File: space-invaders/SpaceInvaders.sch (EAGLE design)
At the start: 26 parts

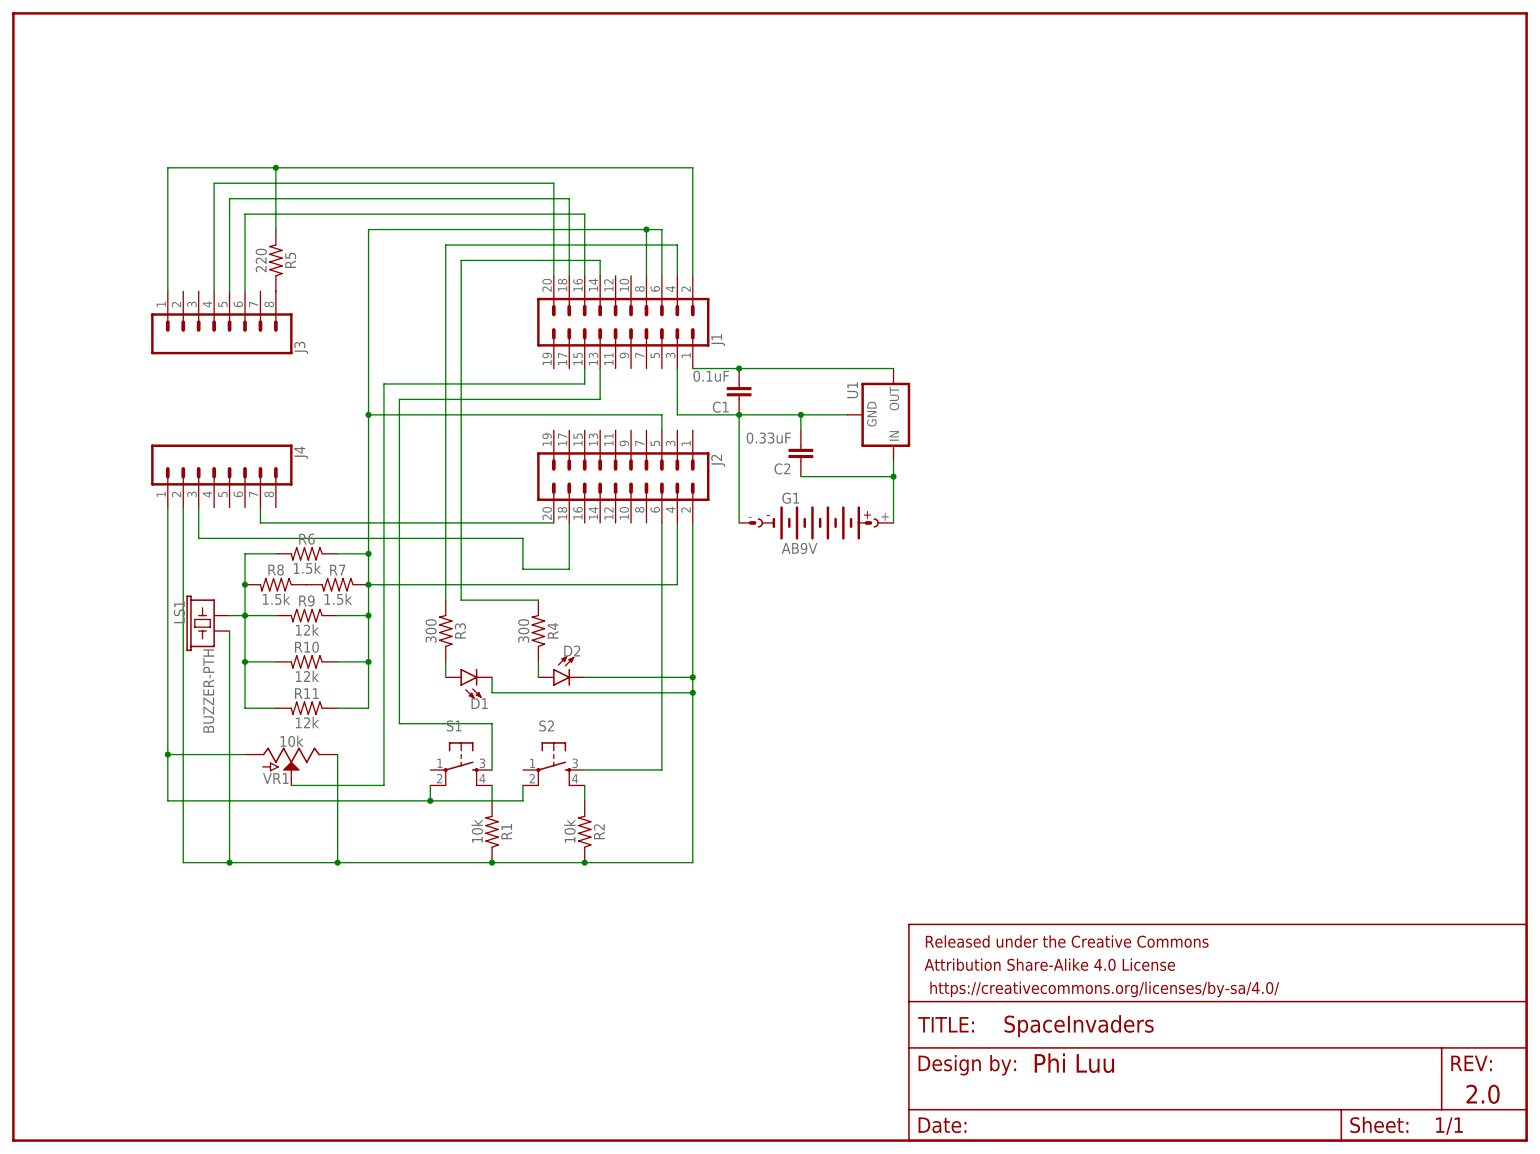
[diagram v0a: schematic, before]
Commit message: Complete board - SpaceInvaders 2.0
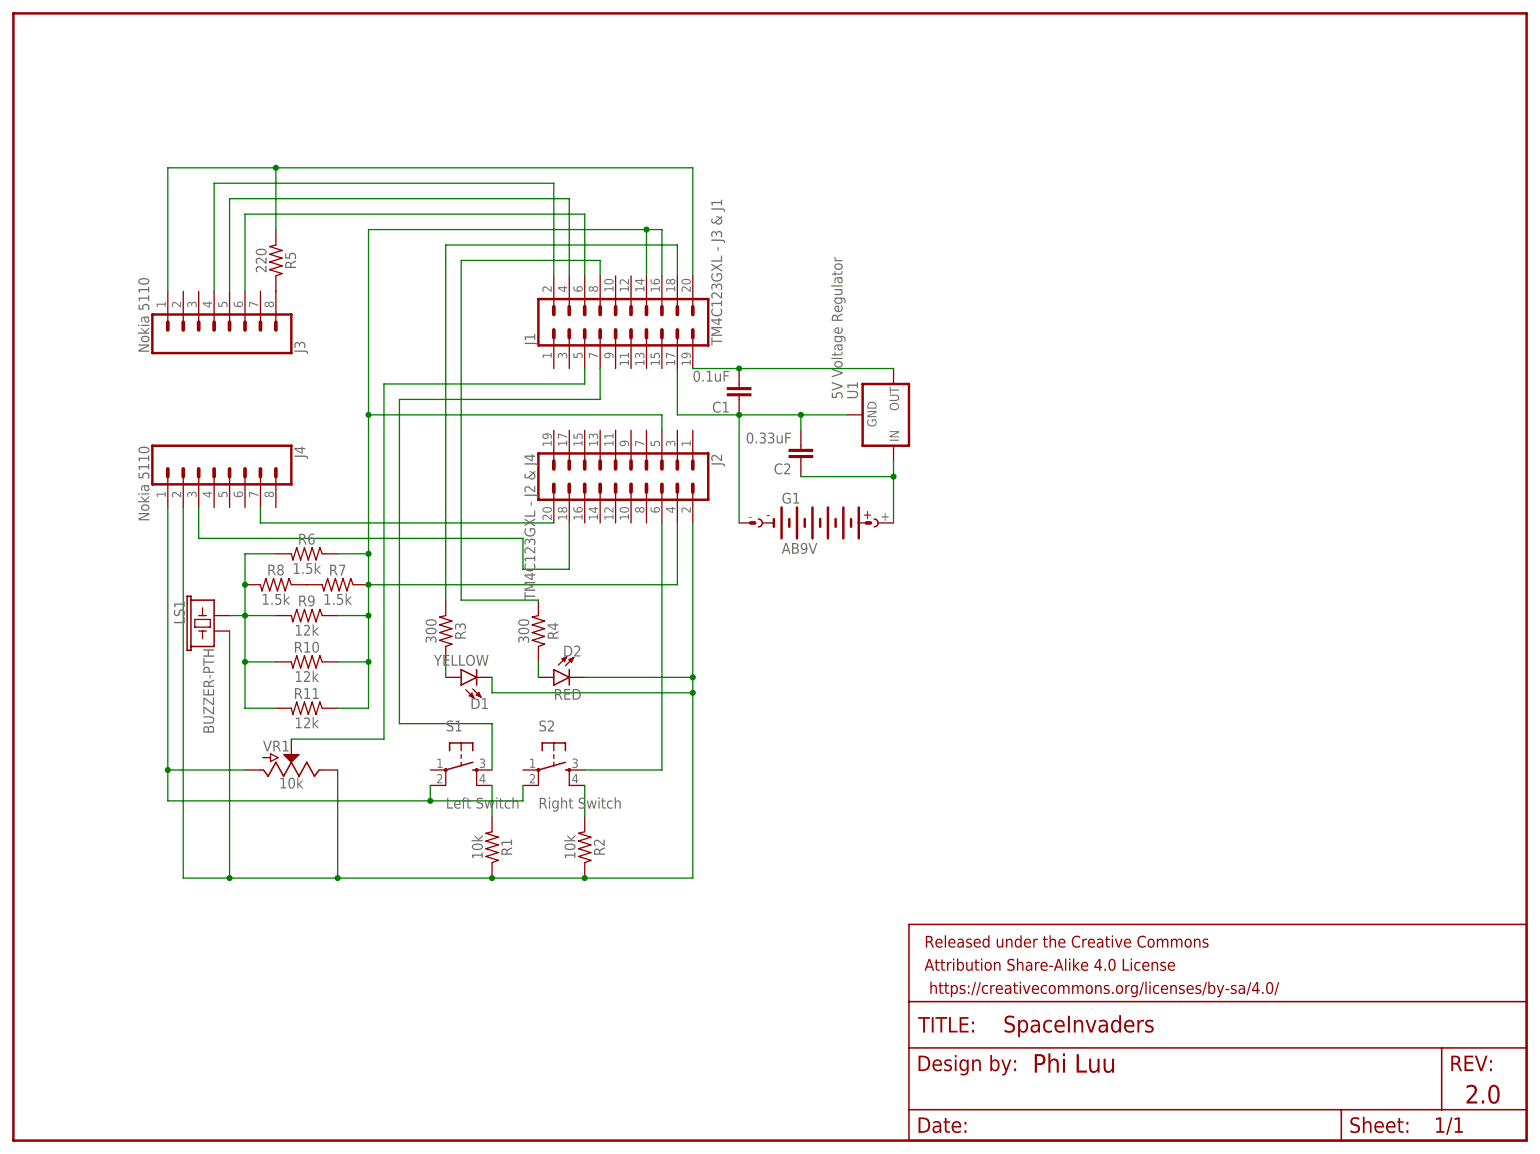
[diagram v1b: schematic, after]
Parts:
- D1: value (none) -> YELLOW; device SparkFun-LED:LED3MM -> SparkFun-LED:LED5MM
- D2: value (none) -> RED; device SparkFun-LED:LED3MM -> SparkFun-LED:LED5MM
- J1: value (none) -> TM4C123GXL - J3 & J1
- J2: value (none) -> TM4C123GXL - J2 & J4
- J3, J4: value (none) -> Nokia 5110
- S1: value (none) -> Left Switch
- S2: value (none) -> Right Switch
- U1: value (none) -> 5V Voltage Regulator
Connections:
- net N$12: now also J1.2; no longer J1.20
- net N$13: now also J1.4; no longer J1.18
- net N$15: now also J1.6; no longer J1.16
- net N$17: now also J1.5; no longer J1.15
- net N$19: now also J1.7; no longer J1.13
- net N$21: now also J1.18; no longer J1.4
- net N$22: now also J1.8; no longer J1.14
- net N$24: now also J1.19; no longer J1.1
- net N$25: now also J1.17; no longer J1.3
- net N$5: now also J1.14, J1.16; no longer J1.6, J1.8
- net N$9: now also J1.20; no longer J1.2
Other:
- moved on the sheet: R1, R2, VR1

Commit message: Add silkscreen & Finish SpaceInvaders
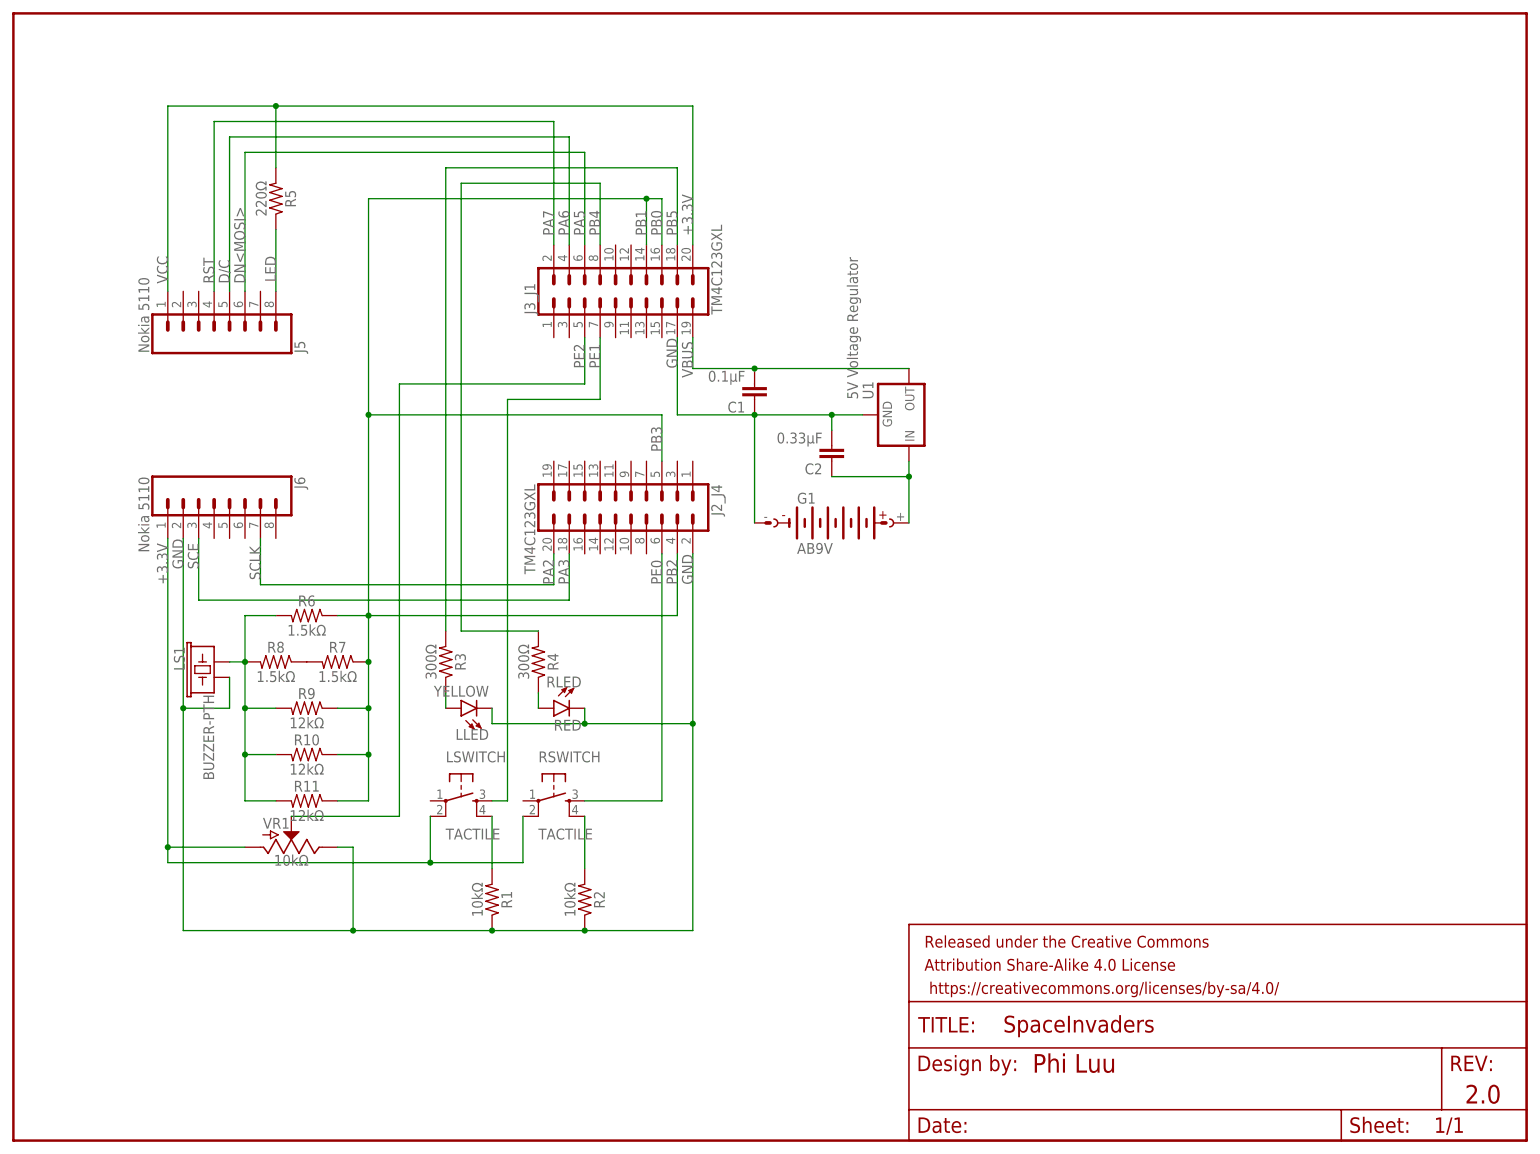
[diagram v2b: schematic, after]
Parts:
- removed D1: YELLOW, SparkFun-LED:LED5MM
- removed D2: RED, SparkFun-LED:LED5MM
- removed J1: TM4C123GXL - J3 & J1, SparkFun-Connectors:CONN_10X2
- removed J2: TM4C123GXL - J2 & J4, SparkFun-Connectors:CONN_10X2
- removed J4: Nokia 5110, SparkFun-Connectors:CONN_08"
- removed S1: Left Switch, SparkFun-Retired:TAC_SWITCHPTH
- removed S2: Right Switch, SparkFun-Retired:TAC_SWITCHPTH
- added J2_J4, J3_J1: TM4C123GXL, SparkFun-Connectors:CONN_10X2
- added J6: Nokia 5110, SparkFun-Connectors:CONN_08"
- added LLED: YELLOW, SparkFun-LED:LED5MM
- added LSWITCH, RSWITCH: TACTILE, SparkFun-Retired:TAC_SWITCHPTH
- added RLED: RED, SparkFun-LED:LED5MM
- C1: value 0.1uF -> 0.1μF
- C2: value 0.33uF -> 0.33μF
- R1, R2, VR1: value 10k -> 10kΩ
- R10, R11, R9: value 12k -> 12kΩ
- R3, R4: value 300 -> 300Ω
- R5: value 220 -> 220Ω
- R6, R7, R8: value 1.5k -> 1.5kΩ
- renumbered J3 to J5
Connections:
- net N$3 renamed LED
- removed net N$1 (its old number): R1.2, S1.4
- removed net N$10: J4.1, S1.2, S2.2, VR1.A
- removed net N$11: D1.C, D2.C, J2.2, J4.2, LS1.2, R1.1, R2.1, VR1.E
- removed net N$13: J1.4, J5.5
- removed net N$15: J1.6, J5.6
- removed net N$16: J2.20, J4.7
- removed net N$2: R2.2, S2.4
- removed net N$20: J2.6, S2.3
- removed net N$21: J1.18, R3.2
- removed net N$22: J1.8, R4.2
- removed net N$24 (its old number): C1.2, J1.19, U1.OUT
- removed net N$25: C1.1, C2.2, G1.-, J1.17, U1.GND
- removed net N$5: J1.14, J1.16, J2.4, J2.5, R10.1, R11.1, R6.1, R7.1, R9.1
- removed net N$7: D1.A, R3.1
- removed net N$8: D2.A, R4.1
- removed net N$9: J1.20, J5.1, R5.2
- new net +3.3V: J3_J1.20, J5.1, J6.1, LSWITCH.2, R5.2, RSWITCH.2, VR1.A
- new net GND: C1.1, C2.2, G1.-, J2_J4.2, J3_J1.17, J6.2, LLED.C, LS1.2, R1.1, R2.1, RLED.C, U1.GND, VR1.E
- new net PA2: J2_J4.20, J6.7
- new net PA3: J2_J4.18, J6.3
- new net PA5: J3_J1.6, J5.6
- new net PA6: J3_J1.4, J5.5
- new net PA7: J3_J1.2, J5.4
- new net PB2: J2_J4.4, J2_J4.5, J3_J1.14, J3_J1.16, R10.1, R11.1, R6.1, R7.1, R9.1
- new net PB4: J3_J1.8, R4.2
- new net PB5: J3_J1.18, R3.2
- new net PE0: J2_J4.6, RSWITCH.3
- new net PE1: J3_J1.7, LSWITCH.3
- new net PE2: J3_J1.5, VR1.S
- new net VBUS: C1.2, J3_J1.19, U1.OUT
- net N$12: now also LSWITCH.4, R1.2; no longer J1.2, J5.4
- net N$14: now also R2.2, RSWITCH.4; no longer J2.18, J4.3
- net N$17: now also R4.1, RLED.A; no longer J1.5, VR1.S
- net N$19: now also LLED.A, R3.1; no longer J1.7, S1.3
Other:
- note added: "D/C"
- note added: "DN<MOSI>"
- note added: "PB0"
- note added: "PB1"
- note added: "PB3"
- note added: "RST"
- note added: "SCE"
- note added: "SCLK"
- note added: "VCC"
- moved on the sheet: C1, C2, G1, LS1, R1, R10, R11, R2, R3, R4, R5, R6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
